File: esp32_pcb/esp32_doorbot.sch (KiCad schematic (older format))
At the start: 20 parts, among them J1 Conn_01x07_Male, J2 Conn_01x02_Female, J3 Barrel_Jack, J4 WROOM32_1, J5 WROOM32_2, Q1 ZXMP4A16G, U1 L7805

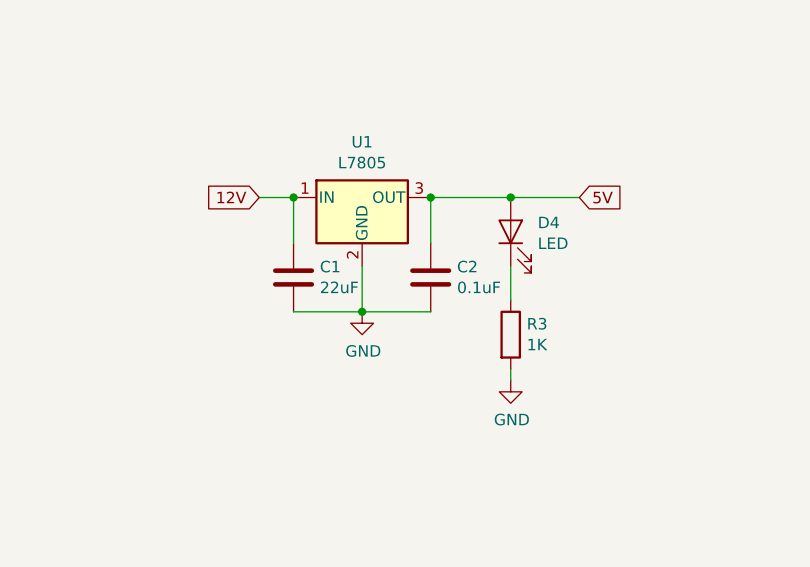
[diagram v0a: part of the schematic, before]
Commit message: Use a through-hole buck converter
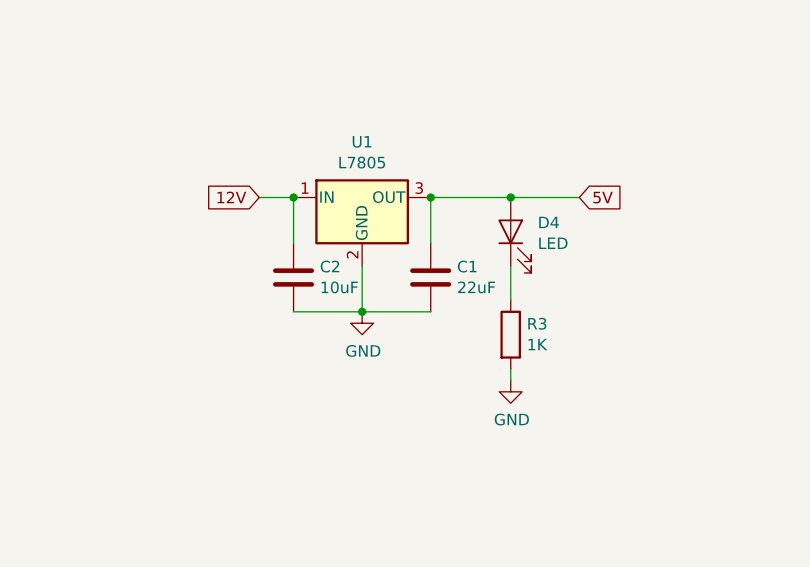
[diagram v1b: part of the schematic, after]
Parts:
- C2: value 0.1uF -> 10uF; Digikey # 478-1529-2-ND -> 1276-6736-1-ND
- U1: footprint TO_SOT_Packages_SMD:TO-252-2Lead -> TO_SOT_Packages_THT:TO-220_Neutral123_Vertical; Digikey # 497-7255-2-ND -> 1470-VR10S05-ND
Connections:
- net 12V: now also C2.1; no longer C1.1
- net 5V: now also C1.1; no longer C2.1
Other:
- moved on the sheet: C1
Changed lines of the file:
@@
 F 0 "U1" H 4850 3192 50  0000 C CNN
 F 1 "L7805" H 4850 3101 50  0000 C CNN
-F 2 "TO_SOT_Packages_SMD:TO-252-2Lead" H 4875 2800 50  0001 L CIN
+F 2 "TO_SOT_Packages_THT:TO-220_Neutral123_Vertical" H 4875 2800 50  0001 L CIN
 F 3 "http://www.st.com/content/ccc/resource/technical/document/datasheet/41/4f/b3/b0/12/d4/47/88/CD00000444.pdf/files/CD00000444.pdf/jcr:content/translations/en.CD00000444.pdf" H 4850 2900 50  0001 C CNN
-F 4 "497-7255-2-ND" H 4850 2950 50  0001 C CNN "Digikey #"
+F 4 "1470-VR10S05-ND" H 4850 2950 50  0001 C CNN "Digikey #"
 	1    4850 2950
 	1    0    0    -1
@@
 L Device:C C1
 U 1 1 606078C6
-P 4550 3300
-F 0 "C1" H 4665 3346 50  0000 L CNN
-F 1 "22uF" H 4665 3255 50  0000 L CNN
-F 2 "Capacitors_SMD:C_1206" H 4588 3150 50  0001 C CNN
-F 3 "~" H 4550 3300 50  0001 C CNN
-F 4 "1276-1771-2-ND" H 4550 3300 50  0001 C CNN "Digikey #"
-	1    4550 3300
+P 5150 3300
+F 0 "C1" H 5265 3346 50  0000 L CNN
+F 1 "22uF" H 5265 3255 50  0000 L CNN
+F 2 "Capacitors_SMD:C_1206" H 5188 3150 50  0001 C CNN
+F 3 "~" H 5150 3300 50  0001 C CNN
+F 4 "1276-1771-2-ND" H 5150 3300 50  0001 C CNN "Digikey #"
+	1    5150 3300
 	1    0    0    -1
 $EndComp
@@
 	4850 3450 5150 3450
 Connection ~ 4850 3450
-Wire Wire Line
-	4850 3450 4550 3450
 Text GLabel 4400 2950 0    50   Input ~ 0
 12V
@@
 	3400 5750 3400 5900
 $Comp
-L Device:C C2
-U 1 1 60E33917
-P 5150 3300
-F 0 "C2" H 5265 3346 50  0000 L CNN
-F 1 "0.1uF" H 5265 3255 50  0000 L CNN
-F 2 "Capacitors_SMD:C_1206" H 5188 3150 50  0001 C CNN
-F 3 "~" H 5150 3300 50  0001 C CNN
-F 4 "478-1529-2-ND" H 5150 3300 50  0001 C CNN "Digikey #"
-	1    5150 3300
-	1    0    0    -1
-$EndComp
-$Comp
 L Transistor_FET:ZXMP4A16G Q1
 U 1 1 61512B24
@@
 	1    0    0    -1
 $EndComp
+$Comp
+L Device:C C2
+U 1 1 61517F68
+P 4550 3300
+F 0 "C2" H 4665 3346 50  0000 L CNN
+F 1 "10uF" H 4665 3255 50  0000 L CNN
+F 2 "Capacitors_SMD:C_1206" H 4588 3150 50  0001 C CNN
+F 3 "~" H 4550 3300 50  0001 C CNN
+F 4 "1276-6736-1-ND" H 4550 3300 50  0001 C CNN "Digikey #"
+	1    4550 3300
+	1    0    0    -1
+$EndComp
+Wire Wire Line
+	4550 3450 4850 3450
 $EndSCHEMATC

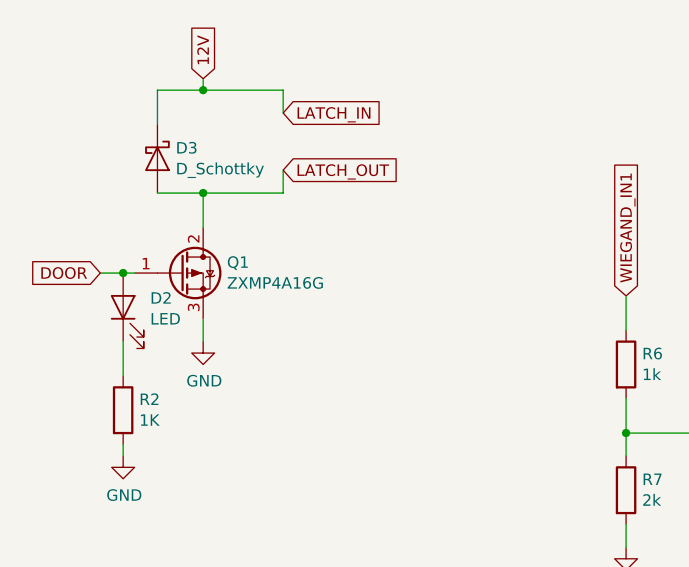
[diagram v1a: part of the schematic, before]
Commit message: New mosfet
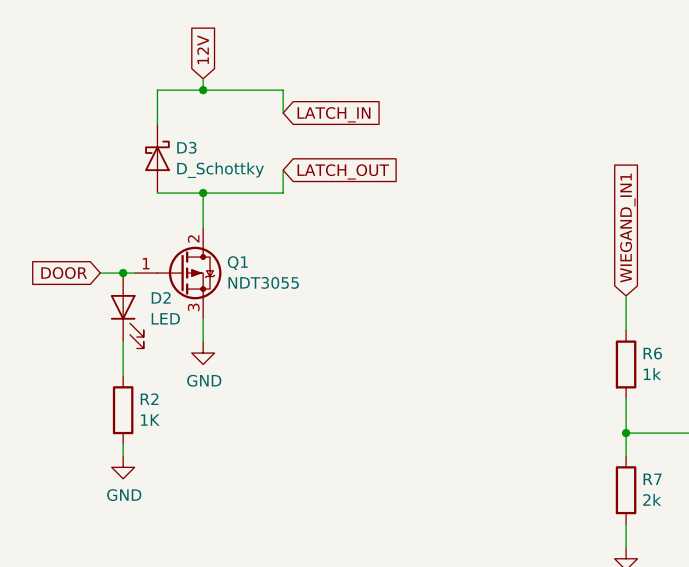
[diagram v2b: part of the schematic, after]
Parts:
- Q1: value ZXMP4A16G -> NDT3055; Digikey # ZVN4206GVTR-ND -> NDT3055CT-ND
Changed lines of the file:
@@
 P 1450 5650
 F 0 "Q1" H 1654 5696 50  0000 L CNN
-F 1 "ZXMP4A16G" H 1654 5605 50  0000 L CNN
+F 1 "NDT3055" H 1654 5605 50  0000 L CNN
 F 2 "TO_SOT_Packages_SMD:SOT-223" H 1650 5575 50  0001 L CIN
-F 3 "https://www.diodes.com/assets/Datasheets/ZXMP4A16G.pdf" H 1450 5650 50  0001 L CNN
-F 4 "ZVN4206GVTR-ND" H 1450 5650 50  0001 C CNN "Digikey #"
+F 3 "https://www.onsemi.com/pdf/datasheet/ndt3055-d.pdf" H 1450 5650 50  0001 L CNN
+F 4 "NDT3055CT-ND" H 1450 5650 50  0001 C CNN "Digikey #"
 	1    1450 5650
 	1    0    0    -1
